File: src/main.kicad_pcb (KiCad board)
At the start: 4 copper layers, 54 parts, among them P301 CONN_01X15, P302 CONN_01X03, P501 CONN_01X07, Q501 MMBT3904, Q502 MMBT3904, U301 LM741, U302 DG444, U303 LM741, U304 LM741, U305 LM311N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

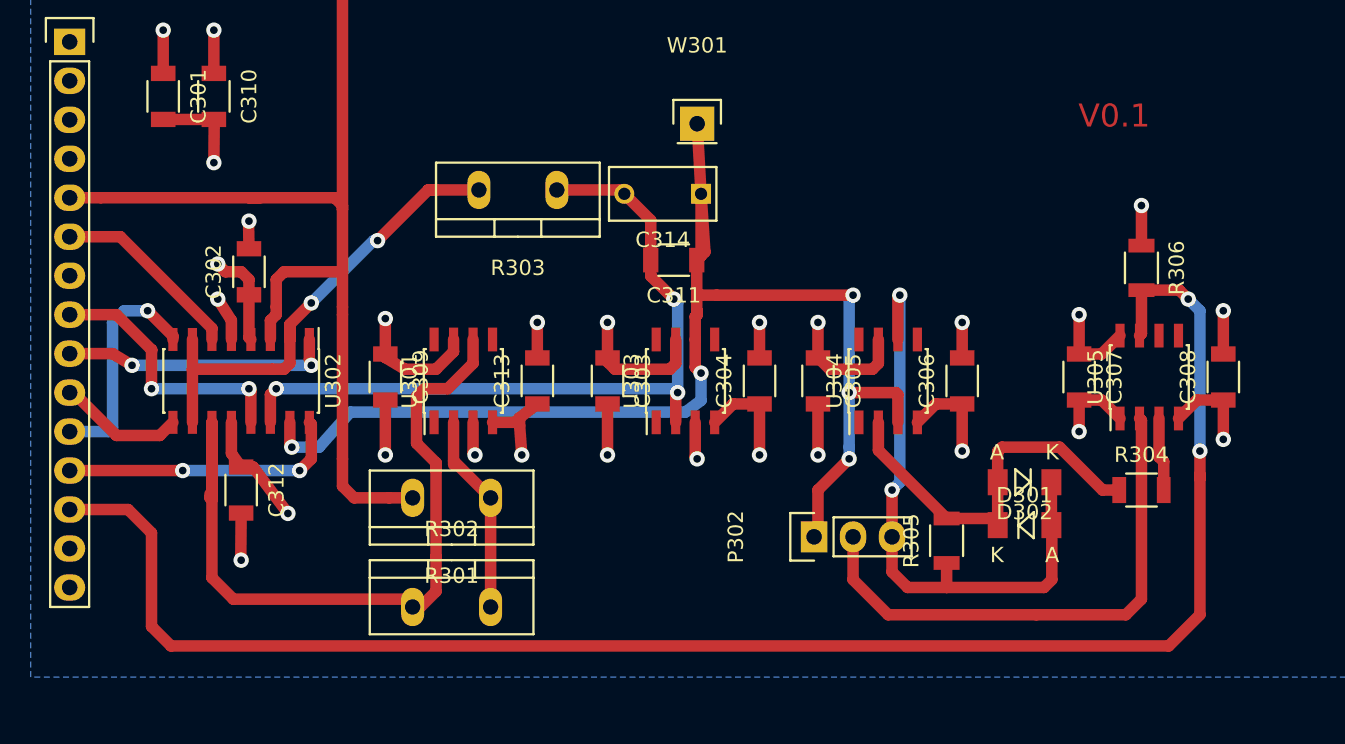
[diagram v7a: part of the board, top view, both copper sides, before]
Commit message: shorter underneath traces
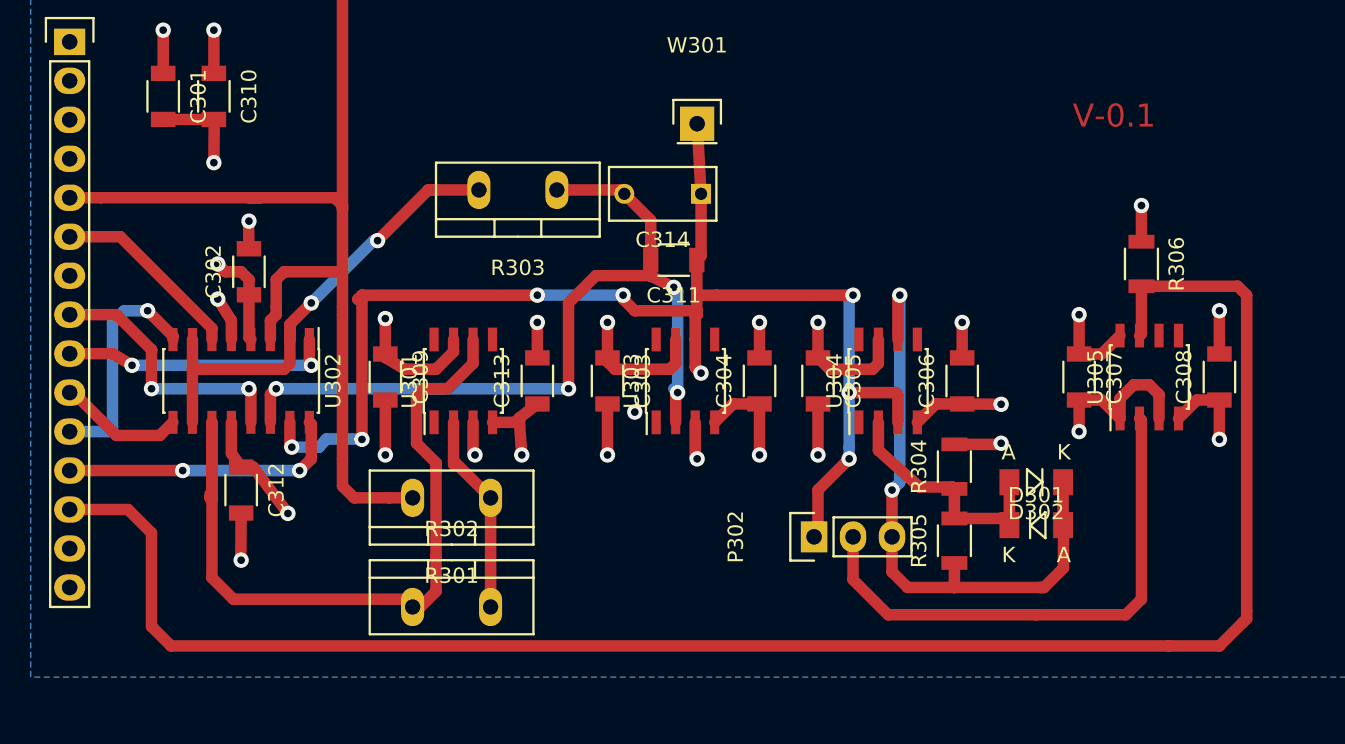
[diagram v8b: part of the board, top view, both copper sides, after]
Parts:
- moved R304 12.3 mm to (101.6, 90.7), turned to 90 degrees
- moved D301 0.76 mm to (106.9, 94.5)
- moved D302 0.76 mm to (106.9, 91.7)
- moved R305 0.51 mm to (101.6, 95.5)
- moved C308 0.25 mm to (118.9, 84.8)
- moved R306 0.25 mm to (113.8, 77.5)
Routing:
- net Net-(D301-Pad1): track 25.9 -> 15.5 mm
- net TRIGGER: track 109.2 -> 116.1 mm, vias 2 -> 0
- net Net-(C311-Pad2): track 49.5 -> 54.6 mm, vias 3 -> 4
- net 0V: track 72.1 -> 76.4 mm, vias 20 -> 21
- net Net-(C311-Pad1): track 86.0 -> 88.7 mm, vias 5 -> 8
- net Net-(D301-Pad2): track 40.2 -> 41.3 mm
- net -VE: track 50.8 -> 50.0 mm
- net (no net): vias 0 -> 1
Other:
- board text added: "V-0.1"
- board text removed: "V0.1"
